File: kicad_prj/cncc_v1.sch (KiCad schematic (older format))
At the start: 0 parts

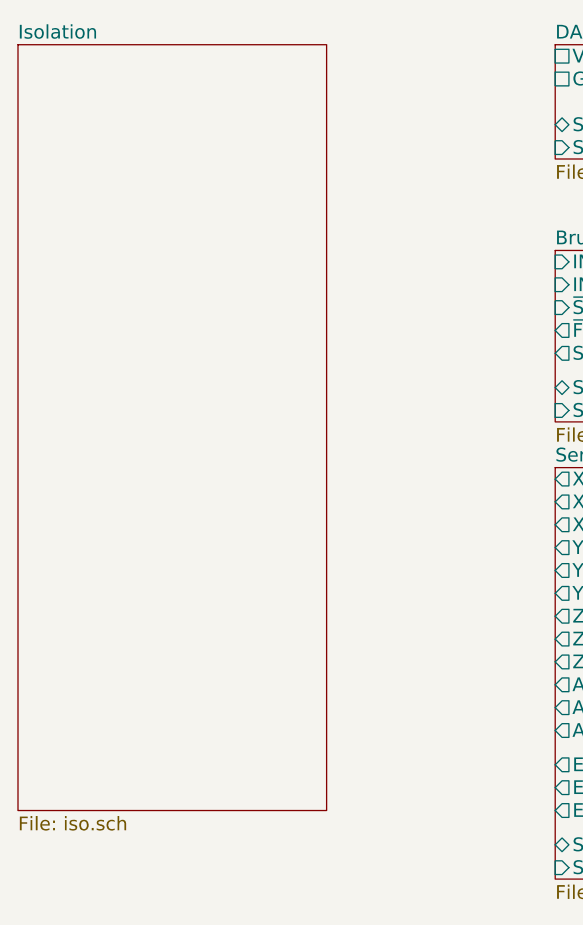
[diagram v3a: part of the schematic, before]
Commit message: Schematics 6
Added isolation.
Misc. i2c, I/Os, spi. Need to finish iso2 sheet.
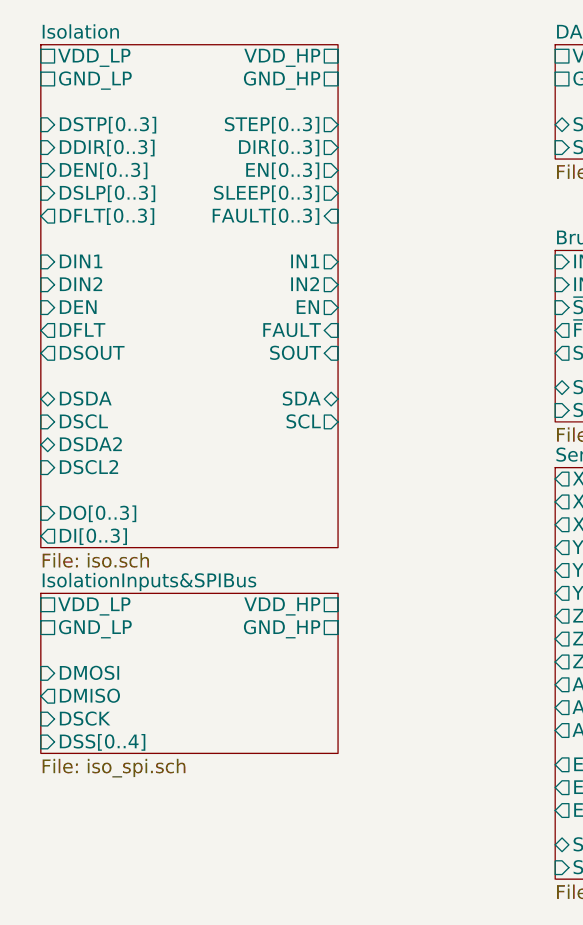
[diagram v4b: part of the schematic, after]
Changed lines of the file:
@@
 $Descr A 11000 8500
 encoding utf-8
-Sheet 1 9
+Sheet 1 10
 Title ""
 Date ""
@@
 F23 "CH7_IN" I R 7800 4400 60
 $EndSheet
+$Sheet
+S 6900 2400 900  500
+U 565650ED
+F0 "DAC" 60
+F1 "dac_out.sch" 60
+F2 "VDD" U L 6900 2450 60
+F3 "GND" U L 6900 2550 60
+F4 "SDA" B L 6900 2750 60
+F5 "SCL" I L 6900 2850 60
+F6 "OUT" O R 7800 2550 60
+$EndSheet
+$Sheet
+S 4650 2400 1300 2200
+U 565A3966
+F0 "Isolation" 60
+F1 "iso.sch" 60
+F2 "STEP[0..3]" O R 5950 2750 60
+F3 "DIR[0..3]" O R 5950 2850 60
+F4 "EN[0..3]" O R 5950 2950 60
+F5 "SLEEP[0..3]" O R 5950 3050 60
+F6 "FAULT[0..3]" I R 5950 3150 60
+F7 "DSTP[0..3]" I L 4650 2750 60
+F8 "DDIR[0..3]" I L 4650 2850 60
+F9 "DEN[0..3]" I L 4650 2950 60
+F10 "DSLP[0..3]" I L 4650 3050 60
+F11 "DFLT[0..3]" O L 4650 3150 60
+F12 "IN2" O R 5950 3450 60
+F13 "IN1" O R 5950 3350 60
+F14 "EN" O R 5950 3550 60
+F15 "DFLT" O L 4650 3650 60
+F16 "DSOUT" O L 4650 3750 60
+F17 "DIN1" I L 4650 3350 60
+F18 "DIN2" I L 4650 3450 60
+F19 "DEN" I L 4650 3550 60
+F20 "FAULT" I R 5950 3650 60
+F21 "SOUT" I R 5950 3750 60
+F22 "SDA" B R 5950 3950 60
+F23 "SCL" O R 5950 4050 60
+F24 "DSDA" B L 4650 3950 60
+F25 "DSCL" I L 4650 4050 60
+F26 "DSCL2" I L 4650 4250 60
+F27 "DSDA2" B L 4650 4150 60
+F28 "DO[0..3]" I L 4650 4450 60
+F29 "DI[0..3]" O L 4650 4550 60
+F30 "VDD_LP" U L 4650 2450 60
+F31 "VDD_HP" U R 5950 2450 60
+F32 "GND_LP" U L 4650 2550 60
+F33 "GND_HP" U R 5950 2550 60
+$EndSheet
 Wire Wire Line
 	7800 4000 8050 4000
@@
 	8100 4400 7800 4400
 $Sheet
-S 6900 2400 900  500
-U 565650ED
-F0 "DAC" 60
-F1 "dac_out.sch" 60
-F2 "VDD" U L 6900 2450 60
-F3 "GND" U L 6900 2550 60
-F4 "SDA" B L 6900 2750 60
-F5 "SCL" I L 6900 2850 60
-F6 "OUT" O R 7800 2550 60
-$EndSheet
-$Sheet
-S 4550 2400 1350 3350
-U 565A3966
-F0 "Isolation" 60
-F1 "iso.sch" 60
+S 4650 4800 1300 700
+U 565FD8F0
+F0 "IsolationInputs&SPIBus" 60
+F1 "iso_spi.sch" 60
+F2 "DSS[0..4]" I L 4650 5450 60
+F3 "DSCK" I L 4650 5350 60
+F4 "DMISO" O L 4650 5250 60
+F5 "DMOSI" I L 4650 5150 60
+F6 "VDD_LP" U L 4650 4850 60
+F7 "GND_LP" U L 4650 4950 60
+F8 "VDD_HP" U R 5950 4850 60
+F9 "GND_HP" U R 5950 4950 60
 $EndSheet
 $EndSCHEMATC

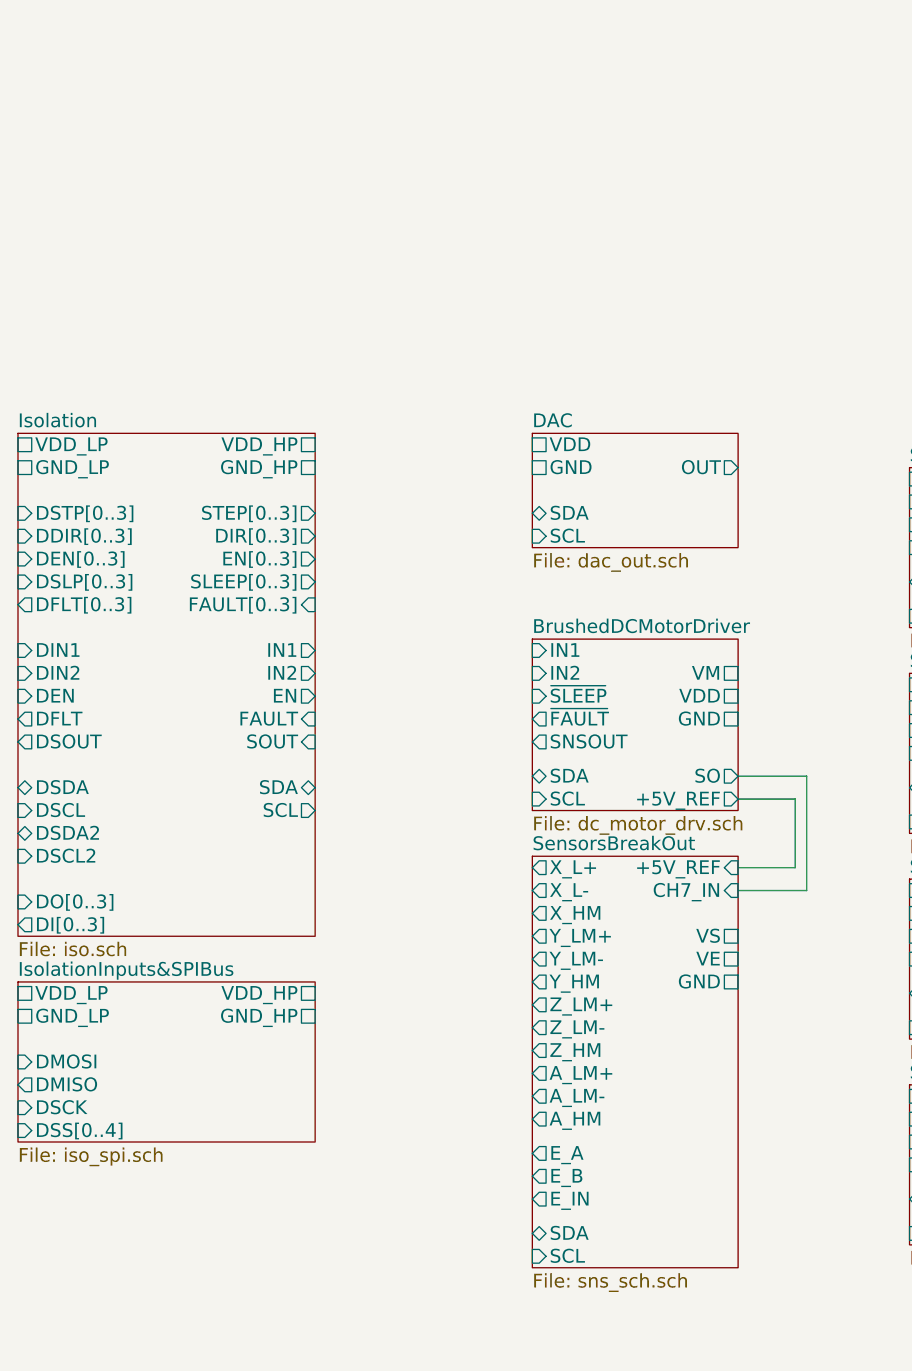
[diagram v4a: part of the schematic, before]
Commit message: Schematics 7
Started power schematics.
Need to:
- correct symbol for sw vreg
- add regulator for 3.3V digital side
- indicate which voltages go to which circuit
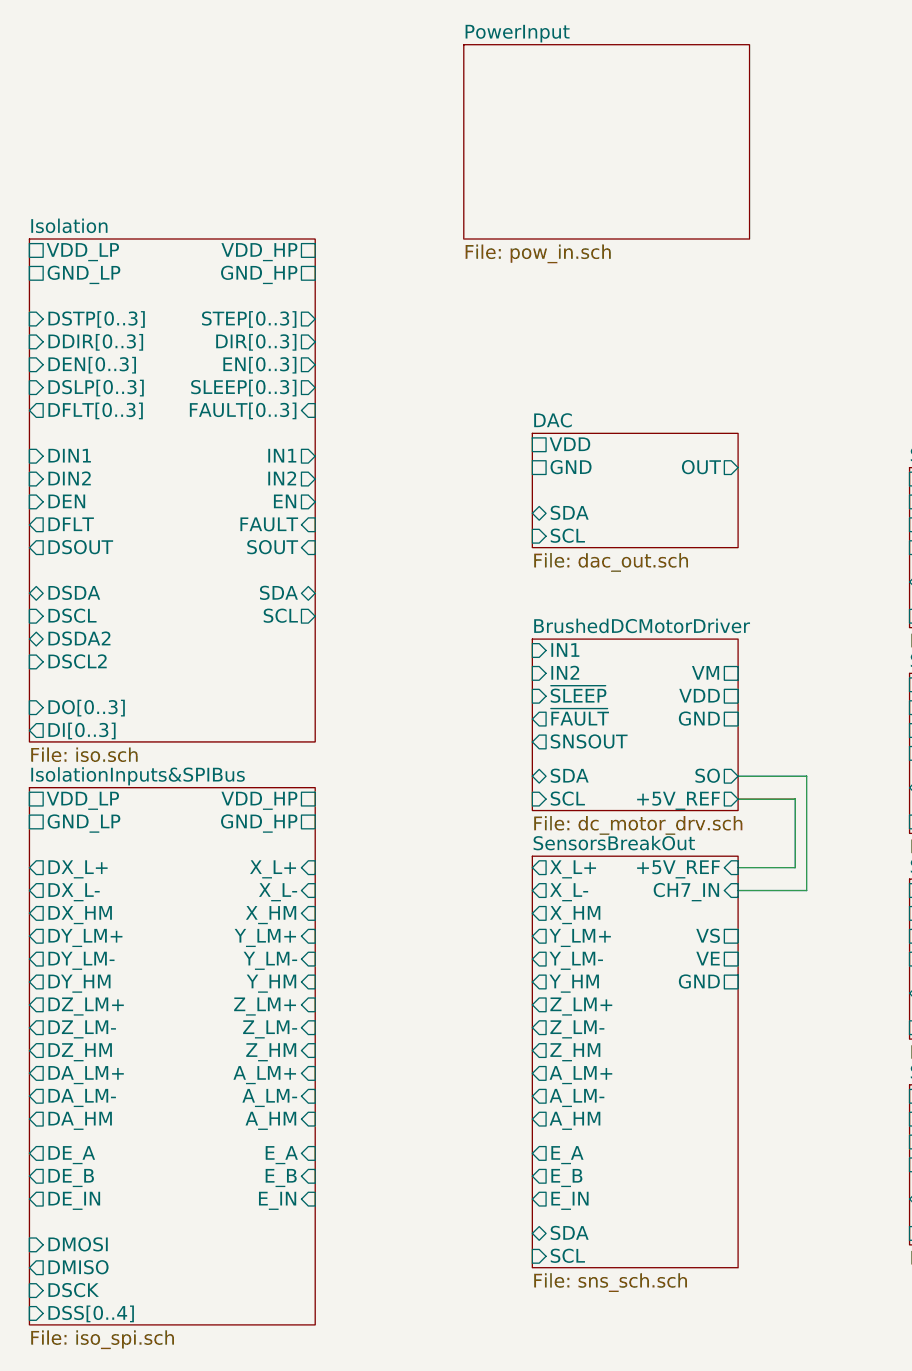
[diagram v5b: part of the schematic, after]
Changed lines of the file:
@@
 $Descr A 11000 8500
 encoding utf-8
-Sheet 1 10
+Sheet 1 11
 Title ""
 Date ""
@@
 $EndSheet
 $Sheet
-S 4650 2400 1300 2200
+S 4700 1550 1250 2200
 U 565A3966
 F0 "Isolation" 60
 F1 "iso.sch" 60
-F2 "STEP[0..3]" O R 5950 2750 60
-F3 "DIR[0..3]" O R 5950 2850 60
-F4 "EN[0..3]" O R 5950 2950 60
-F5 "SLEEP[0..3]" O R 5950 3050 60
-F6 "FAULT[0..3]" I R 5950 3150 60
-F7 "DSTP[0..3]" I L 4650 2750 60
-F8 "DDIR[0..3]" I L 4650 2850 60
-F9 "DEN[0..3]" I L 4650 2950 60
-F10 "DSLP[0..3]" I L 4650 3050 60
-F11 "DFLT[0..3]" O L 4650 3150 60
-F12 "IN2" O R 5950 3450 60
-F13 "IN1" O R 5950 3350 60
-F14 "EN" O R 5950 3550 60
-F15 "DFLT" O L 4650 3650 60
-F16 "DSOUT" O L 4650 3750 60
-F17 "DIN1" I L 4650 3350 60
-F18 "DIN2" I L 4650 3450 60
-F19 "DEN" I L 4650 3550 60
-F20 "FAULT" I R 5950 3650 60
-F21 "SOUT" I R 5950 3750 60
-F22 "SDA" B R 5950 3950 60
-F23 "SCL" O R 5950 4050 60
-F24 "DSDA" B L 4650 3950 60
-F25 "DSCL" I L 4650 4050 60
-F26 "DSCL2" I L 4650 4250 60
-F27 "DSDA2" B L 4650 4150 60
-F28 "DO[0..3]" I L 4650 4450 60
-F29 "DI[0..3]" O L 4650 4550 60
-F30 "VDD_LP" U L 4650 2450 60
-F31 "VDD_HP" U R 5950 2450 60
-F32 "GND_LP" U L 4650 2550 60
-F33 "GND_HP" U R 5950 2550 60
+F2 "STEP[0..3]" O R 5950 1900 60
+F3 "DIR[0..3]" O R 5950 2000 60
+F4 "EN[0..3]" O R 5950 2100 60
+F5 "SLEEP[0..3]" O R 5950 2200 60
+F6 "FAULT[0..3]" I R 5950 2300 60
+F7 "DSTP[0..3]" I L 4700 1900 60
+F8 "DDIR[0..3]" I L 4700 2000 60
+F9 "DEN[0..3]" I L 4700 2100 60
+F10 "DSLP[0..3]" I L 4700 2200 60
+F11 "DFLT[0..3]" O L 4700 2300 60
+F12 "IN2" O R 5950 2600 60
+F13 "IN1" O R 5950 2500 60
+F14 "EN" O R 5950 2700 60
+F15 "DFLT" O L 4700 2800 60
+F16 "DSOUT" O L 4700 2900 60
+F17 "DIN1" I L 4700 2500 60
+F18 "DIN2" I L 4700 2600 60
+F19 "DEN" I L 4700 2700 60
+F20 "FAULT" I R 5950 2800 60
+F21 "SOUT" I R 5950 2900 60
+F22 "SDA" B R 5950 3100 60
+F23 "SCL" O R 5950 3200 60
+F24 "DSDA" B L 4700 3100 60
+F25 "DSCL" I L 4700 3200 60
+F26 "DSCL2" I L 4700 3400 60
+F27 "DSDA2" B L 4700 3300 60
+F28 "DO[0..3]" I L 4700 3600 60
+F29 "DI[0..3]" O L 4700 3700 60
+F30 "VDD_LP" U L 4700 1600 60
+F31 "VDD_HP" U R 5950 1600 60
+F32 "GND_LP" U L 4700 1700 60
+F33 "GND_HP" U R 5950 1700 60
 $EndSheet
 Wire Wire Line
@@
 	8100 4400 7800 4400
 $Sheet
-S 4650 4800 1300 700
+S 4700 3950 1250 2350
 U 565FD8F0
 F0 "IsolationInputs&SPIBus" 60
 F1 "iso_spi.sch" 60
-F2 "DSS[0..4]" I L 4650 5450 60
-F3 "DSCK" I L 4650 5350 60
-F4 "DMISO" O L 4650 5250 60
-F5 "DMOSI" I L 4650 5150 60
-F6 "VDD_LP" U L 4650 4850 60
-F7 "GND_LP" U L 4650 4950 60
-F8 "VDD_HP" U R 5950 4850 60
-F9 "GND_HP" U R 5950 4950 60
+F2 "DSS[0..4]" I L 4700 6250 60
+F3 "DSCK" I L 4700 6150 60
+F4 "DMISO" O L 4700 6050 60
+F5 "DMOSI" I L 4700 5950 60
+F6 "VDD_LP" U L 4700 4000 60
+F7 "GND_LP" U L 4700 4100 60
+F8 "VDD_HP" U R 5950 4000 60
+F9 "GND_HP" U R 5950 4100 60
+F10 "DX_L+" O L 4700 4300 60
+F11 "DX_L-" O L 4700 4400 60
+F12 "DX_HM" O L 4700 4500 60
+F13 "DY_LM+" O L 4700 4600 60
+F14 "DY_LM-" O L 4700 4700 60
+F15 "DY_HM" O L 4700 4800 60
+F16 "DZ_LM+" O L 4700 4900 60
+F17 "DZ_LM-" O L 4700 5000 60
+F18 "DZ_HM" O L 4700 5100 60
+F19 "DA_LM+" O L 4700 5200 60
+F20 "DA_LM-" O L 4700 5300 60
+F21 "DA_HM" O L 4700 5400 60
+F22 "DE_A" O L 4700 5550 60
+F23 "DE_B" O L 4700 5650 60
+F24 "DE_IN" O L 4700 5750 60
+F25 "X_L+" I R 5950 4300 60
+F26 "X_L-" I R 5950 4400 60
+F27 "X_HM" I R 5950 4500 60
+F28 "Y_LM+" I R 5950 4600 60
+F29 "Y_LM-" I R 5950 4700 60
+F30 "Y_HM" I R 5950 4800 60
+F31 "Z_LM+" I R 5950 4900 60
+F32 "Z_LM-" I R 5950 5000 60
+F33 "Z_HM" I R 5950 5100 60
+F34 "A_LM+" I R 5950 5200 60
+F35 "A_LM-" I R 5950 5300 60
+F36 "A_HM" I R 5950 5400 60
+F37 "E_A" I R 5950 5550 60
+F38 "E_B" I R 5950 5650 60
+F39 "E_IN" I R 5950 5750 60
+$EndSheet
+$Sheet
+S 6600 700  1250 850
+U 565E910C
+F0 "PowerInput" 60
+F1 "pow_in.sch" 60
 $EndSheet
 $EndSCHEMATC

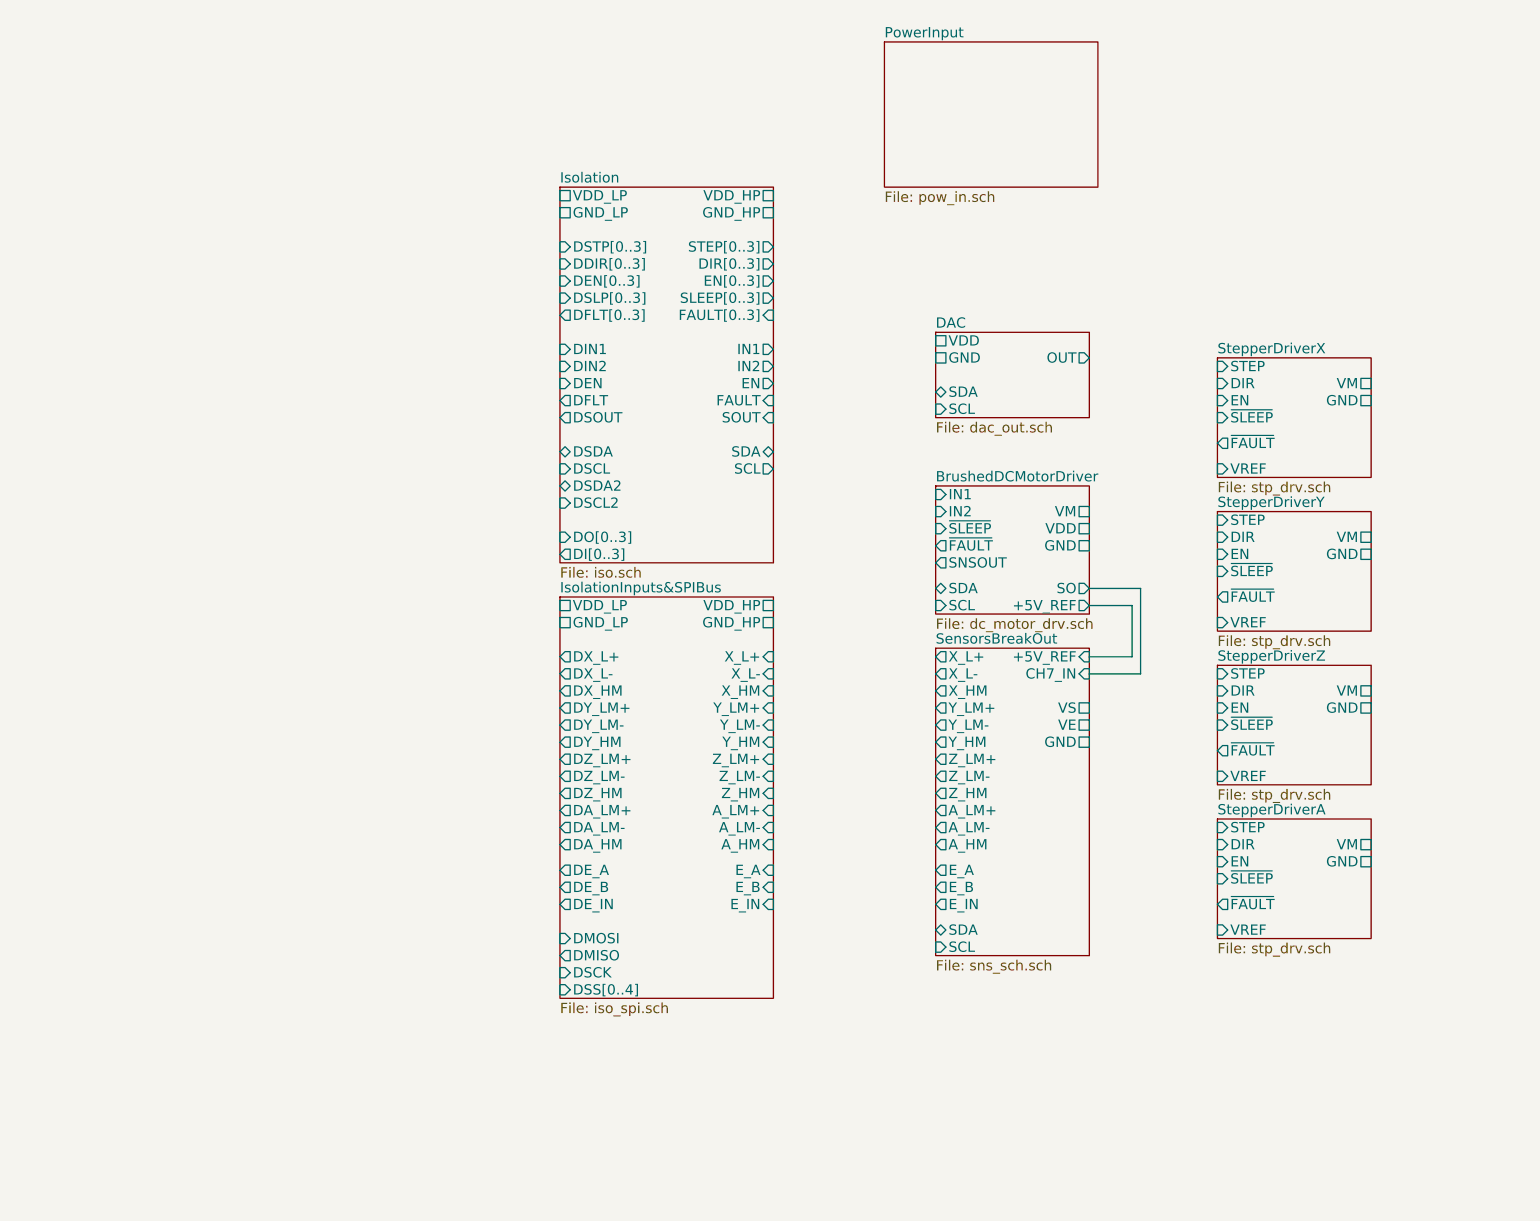
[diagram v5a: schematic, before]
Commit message: Schematics 9
Power circuitry is done.
Need to do MCU circuitry and top level connections.
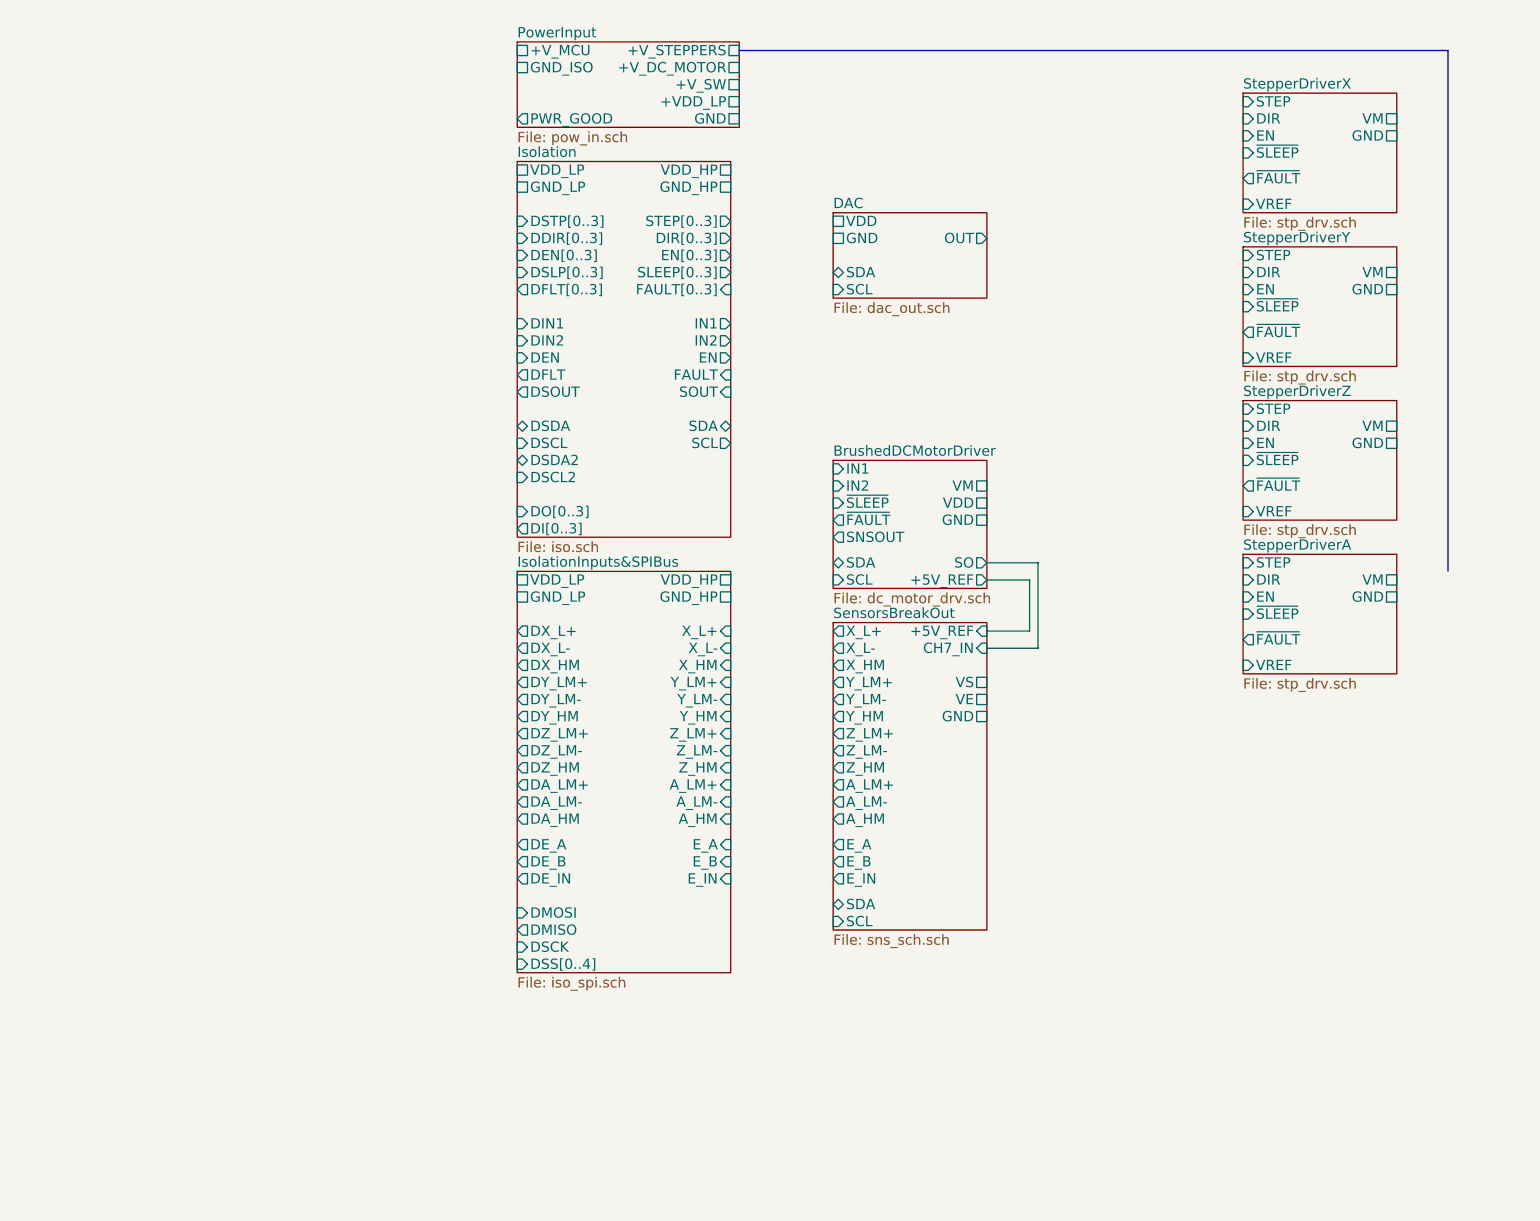
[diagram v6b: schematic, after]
